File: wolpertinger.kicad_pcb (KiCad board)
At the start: 2 copper layers, 121.3 x 130.8 mm, 117 parts, among them J1 RIGHT IN, J2 LEFT IN, J3 EXT LFO, J4 LEFT OUT, J5 RIGHT OUT, J6 Jack-DC, K1 FRT5, K2 FRT5, Q1 BC549, Q2 BC547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

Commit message: layout work
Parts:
- moved C25 48.1 mm to (139.4, 126.0), turned to 90 degrees
- moved C23 42.6 mm to (139.7, 119.1), turned to 90 degrees
- moved C16 41.4 mm to (86.7, 125.2)
- moved R44 41.1 mm to (135.1, 123.2), turned to 180 degrees
- moved C4 40.7 mm to (88.9, 76.2), turned to 0 degrees
- moved C8 38.0 mm to (60.2, 81.3)
- moved R43 37.0 mm to (127.5, 126.2), turned to 0 degrees
- moved C17 35.7 mm to (159.3, 120.4)
- moved R13 34.9 mm to (177.0, 95.2), turned to 180 degrees
- moved D5 34.6 mm to (141.0, 112.0), turned to 180 degrees
- moved C24 31.1 mm to (119.4, 120.9), turned to 180 degrees
- moved C19 30.4 mm to (172.0, 71.6), turned to 0 degrees
- moved R38 30.2 mm to (127.5, 120.1), turned to 0 degrees
- moved R30 29.5 mm to (55.4, 97.0), turned to 0 degrees
- moved R32 28.3 mm to (177.0, 89.2), turned to 180 degrees
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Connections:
- net Vref 3 renamed Vref3
- C18 pad 1: Vref 1 -> Vref1
- C19 pad 1: Vref 2 -> Vref2
- R30 pad 2: Vref 1 -> Vref1
- R31 pad 1: Vref 1 -> Vref1
- R32 pad 2: Vref 2 -> Vref2
- R33 pad 1: Vref 2 -> Vref2
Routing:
- net V1: track 0.00 -> 39.6 mm
- net GND1: track 0.00 -> 38.6 mm
- net LFO out: track 0.00 -> 25.2 mm
- net LFO out inv: track 0.00 -> 24.3 mm
- net 9V: track 0.00 -> 21.9 mm
- net GND: track 0.00 -> 20.6 mm
- net GND3: track 0.00 -> 18.5 mm
- net Net-(SW2B-B): track 0.00 -> 18.4 mm
- net V2: track 0.00 -> 16.3 mm
- net GND2: track 0.00 -> 16.3 mm
- net Net-(R36-Pad2): track 0.00 -> 13.2 mm
- net Net-(R29-Pad2): track 0.00 -> 13.2 mm
- net Net-(SW2A-B): track 0.00 -> 10.5 mm
- net hiL: track 0.00 -> 2.31 mm
- net loL: track 0.00 -> 2.31 mm
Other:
- board size 121.3 x 130.8 mm -> 127.4 x 130.8 mm
- board text removed: "${REFERENCE}"

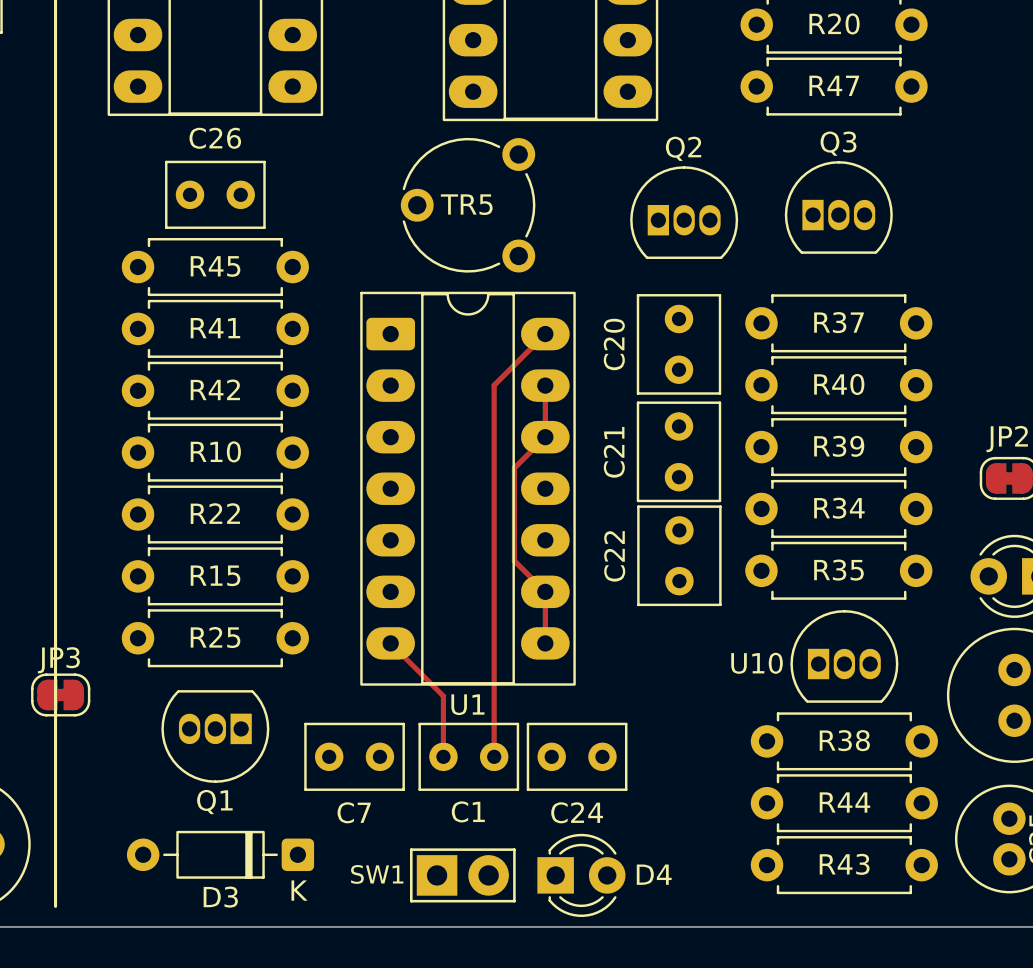
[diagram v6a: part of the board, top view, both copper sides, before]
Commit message: verifiy film cap footprints and transistor footprints
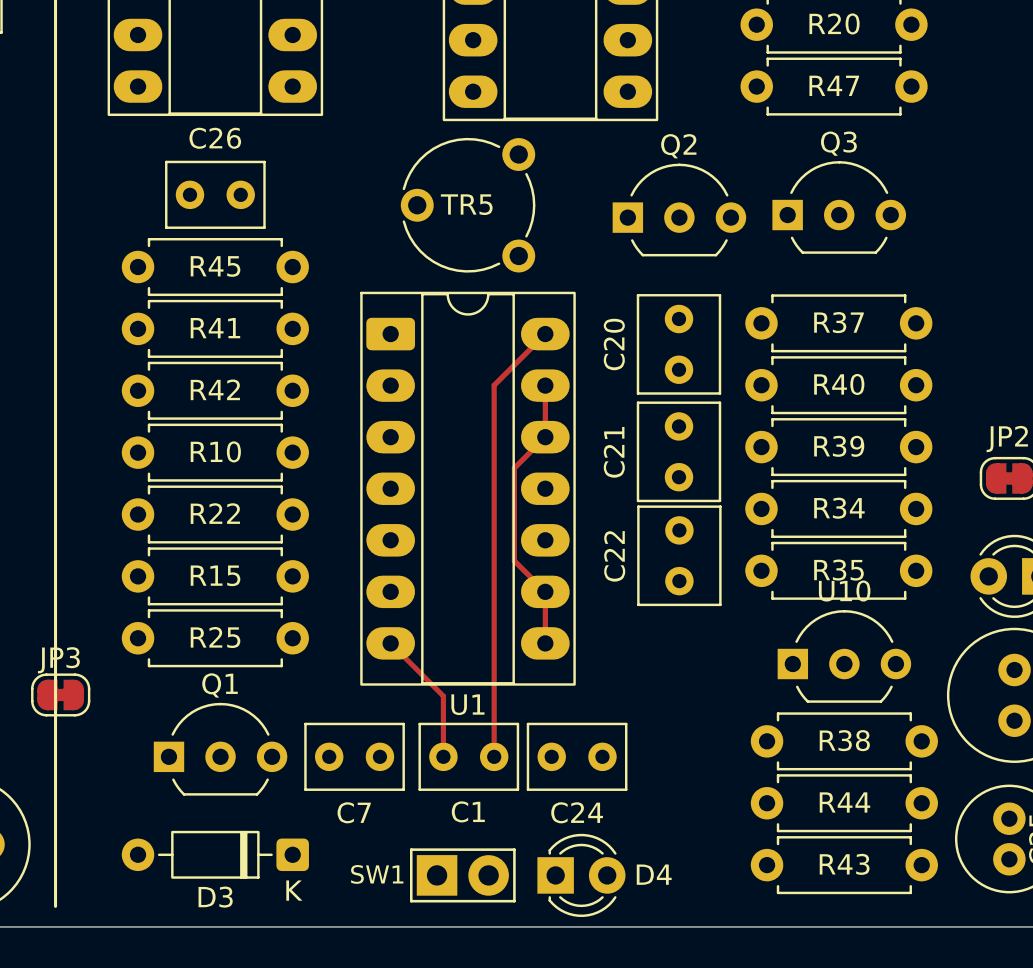
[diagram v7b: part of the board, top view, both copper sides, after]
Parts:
- Q1, Q2, Q3, U10: footprint Package_TO_SOT_THT:TO-92_Inline -> Package_TO_SOT_THT:TO-92_Inline_Wide
- moved Q1 3.81 mm to (98.0, 120.9), turned to 0 degrees
- moved Q2 1.51 mm to (120.7, 94.3)
- moved U10 1.27 mm to (128.8, 116.3)
- moved Q3 1.25 mm to (128.5, 94.2)
- moved D3 0.25 mm to (104.1, 125.7)

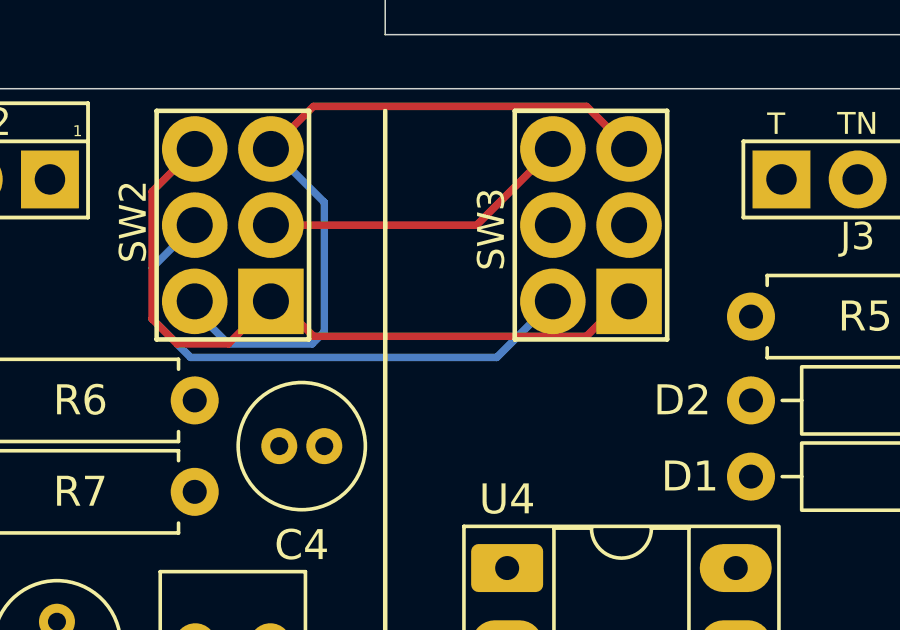
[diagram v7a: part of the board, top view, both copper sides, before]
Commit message: fix short
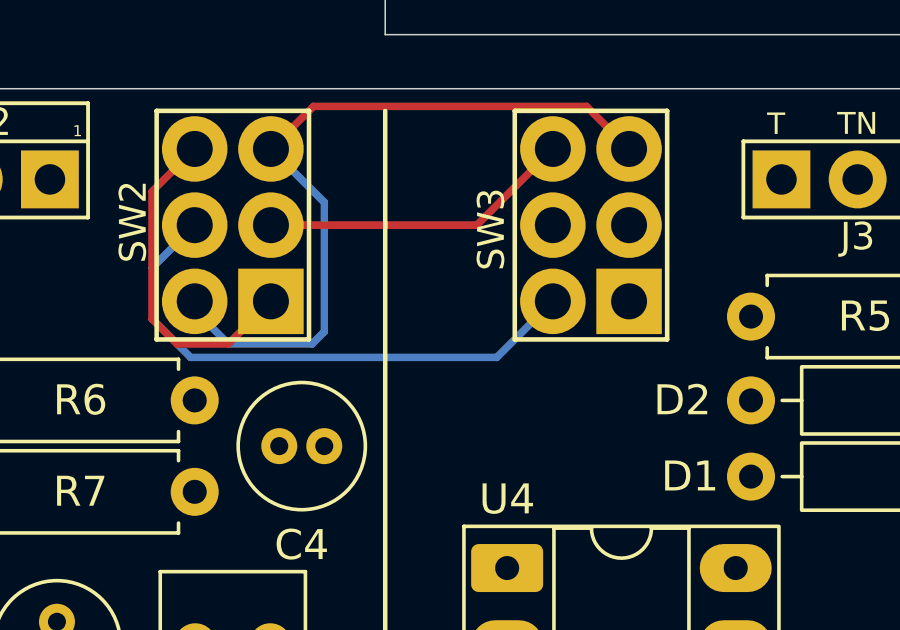
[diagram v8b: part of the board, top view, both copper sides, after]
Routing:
- net LFO out inv: track 24.3 -> 11.1 mm
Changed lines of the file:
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@@
-	)
-	(segment
-		(start 88.646 71.12)
-		(end 90.0642 72.5382)
-		(width 0.25)
-		(layer "F.Cu")
-		(net 22)
 	)
 	(segment
@@
 		(width 0.25)
 		(layer "F.Cu")
-		(net 22)
-	)
-	(segment
-		(start 99.1658 72.5382)
-		(end 100.584 71.12)
-		(width 0.25)
-		(layer "F.Cu")
-		(net 22)
-	)
-	(segment
-		(start 90.0642 72.5382)
-		(end 99.1658 72.5382)
-		(width 0.25)
-		(layer "F.Cu")
